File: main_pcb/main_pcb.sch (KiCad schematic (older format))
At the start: 53 parts, among them J1 DBG, J2 UI, J3 UI, J4 Raspberry_Pi_Zero_WH, J5 UI, J6 UI, J7 UPDN, J8 ISP, J9 BTN_TRIG, Q1 BSS123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

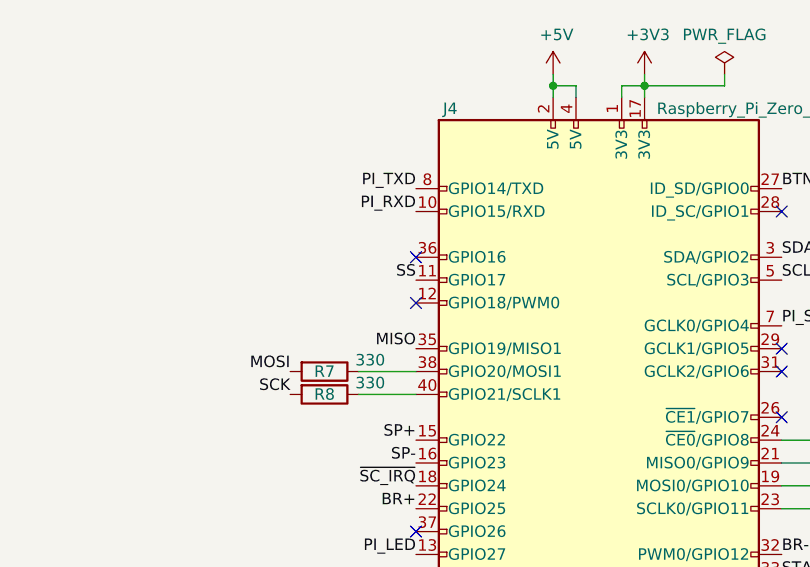
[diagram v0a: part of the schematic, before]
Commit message: Switched SPI to CS0 on RPi
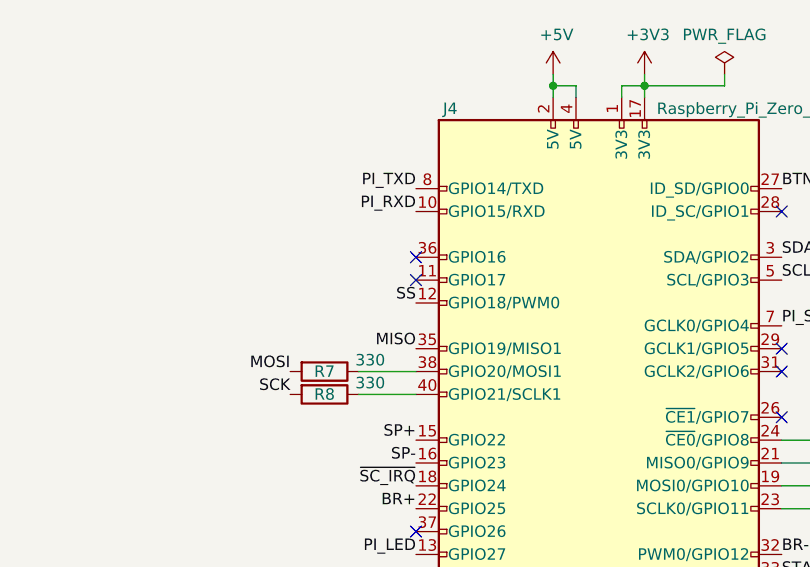
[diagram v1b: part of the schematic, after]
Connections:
- net SS: now also J4.12 (GPIO18/PWM0); no longer J4.11 (GPIO17)
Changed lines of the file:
@@
 Text Label 9650 3000 0    50   ~ 0
 SS
-Text Label 2750 3800 2    50   ~ 0
+Text Label 2750 3900 2    50   ~ 0
 SS
 $Comp
@@
 NoConn ~ 4350 4100
 NoConn ~ 4350 4400
-NoConn ~ 2750 3900
 NoConn ~ 2750 3700
 $Comp
@@
 Wire Wire Line
 	5350 6850 5350 6900
+NoConn ~ 2750 3800
 $EndSCHEMATC

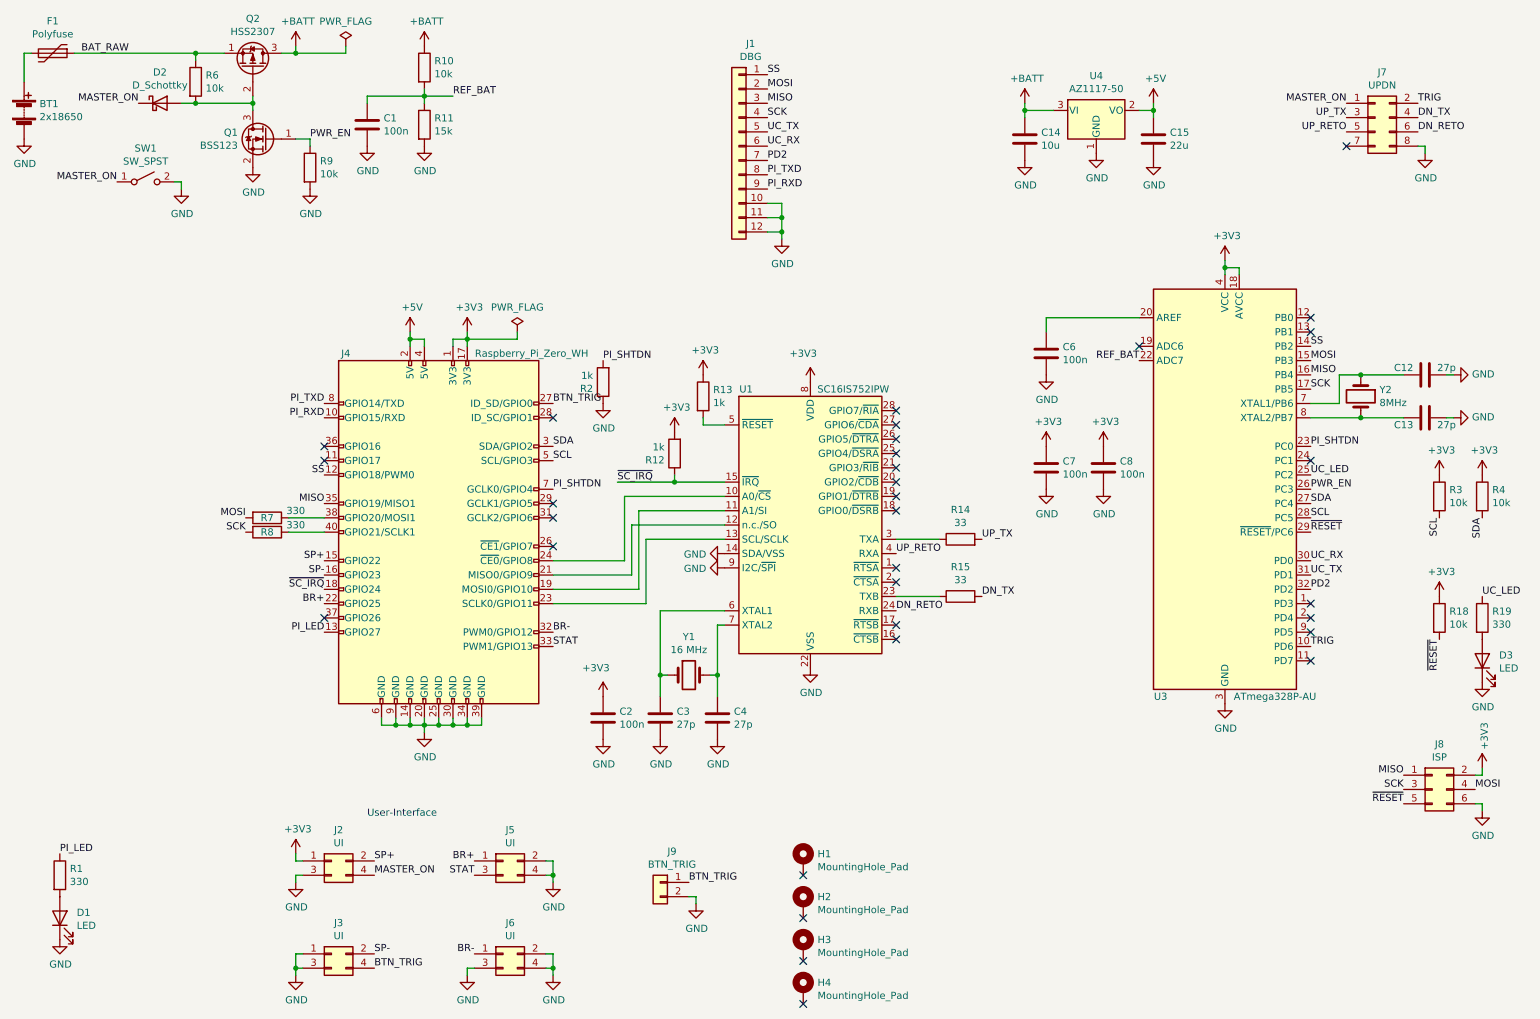
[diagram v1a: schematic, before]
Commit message: Added MASTER_ON wire also to uC over a large resistor to detect button presses while powered on to turn off, cleaned silk screen
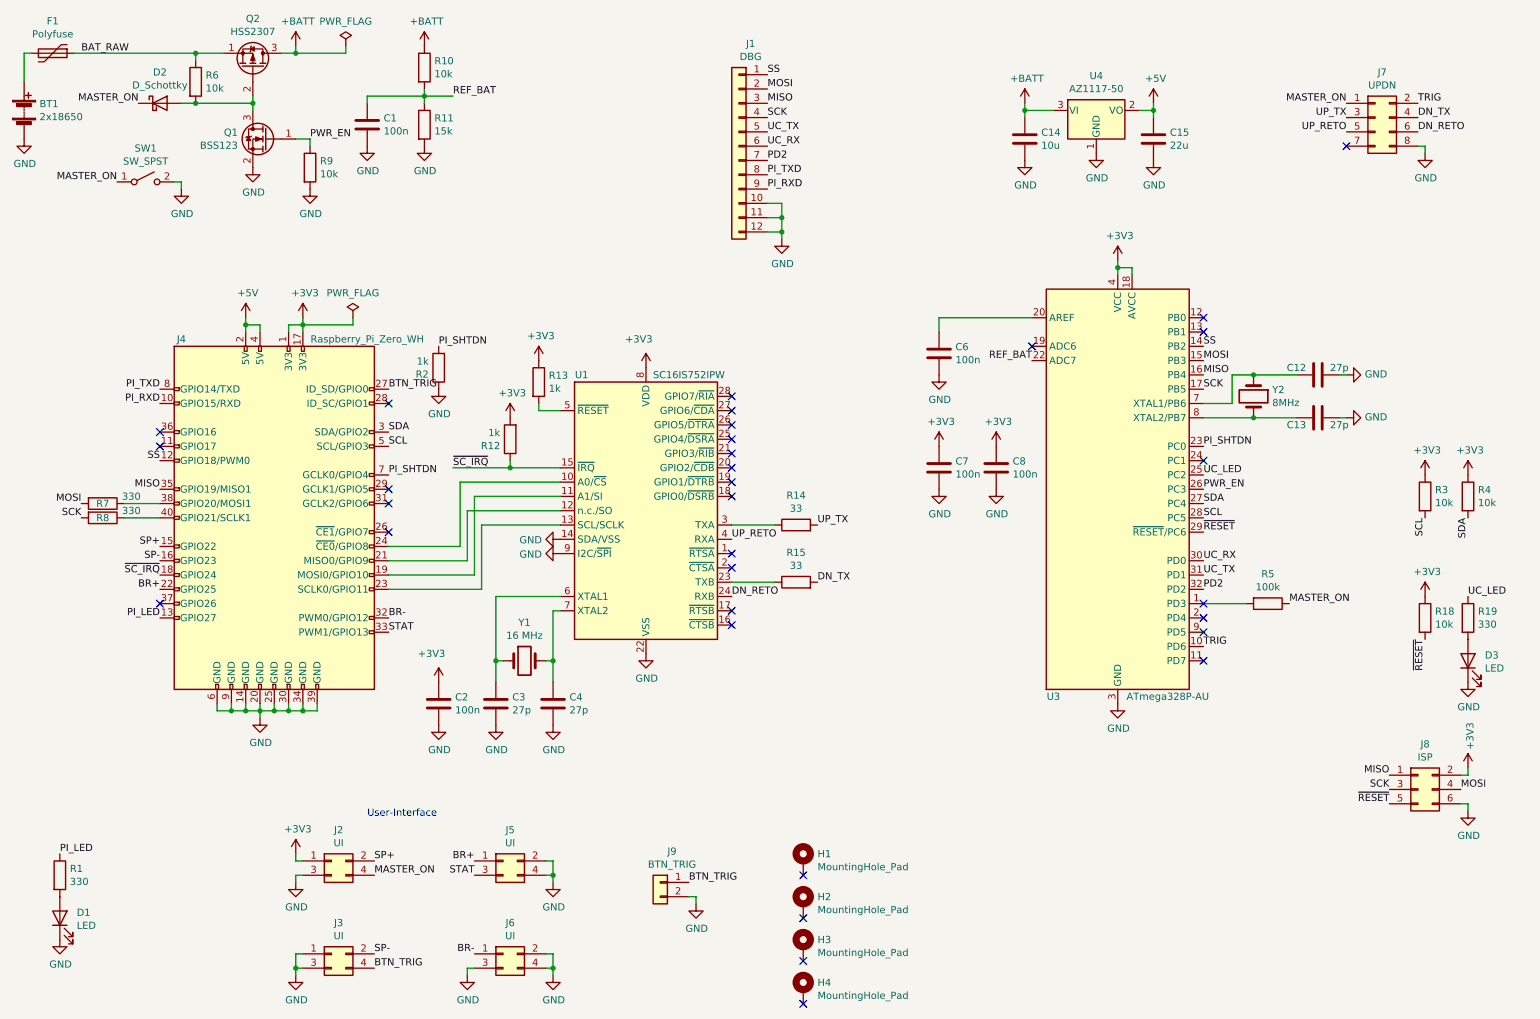
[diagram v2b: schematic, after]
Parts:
- added R5: 100k, Resistor_SMD:R_0603_1608Metric, symbol Device:R
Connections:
- net MASTER_ON: now also R5.1
- net at U3.1 (PD3): now also R5.2
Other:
- moved on the sheet: C12, C13, C2, C3, C4, C6, C7, C8, D3, J4, J8, R12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
